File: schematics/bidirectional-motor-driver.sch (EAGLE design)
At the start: 14 parts, among them IC1 4011D

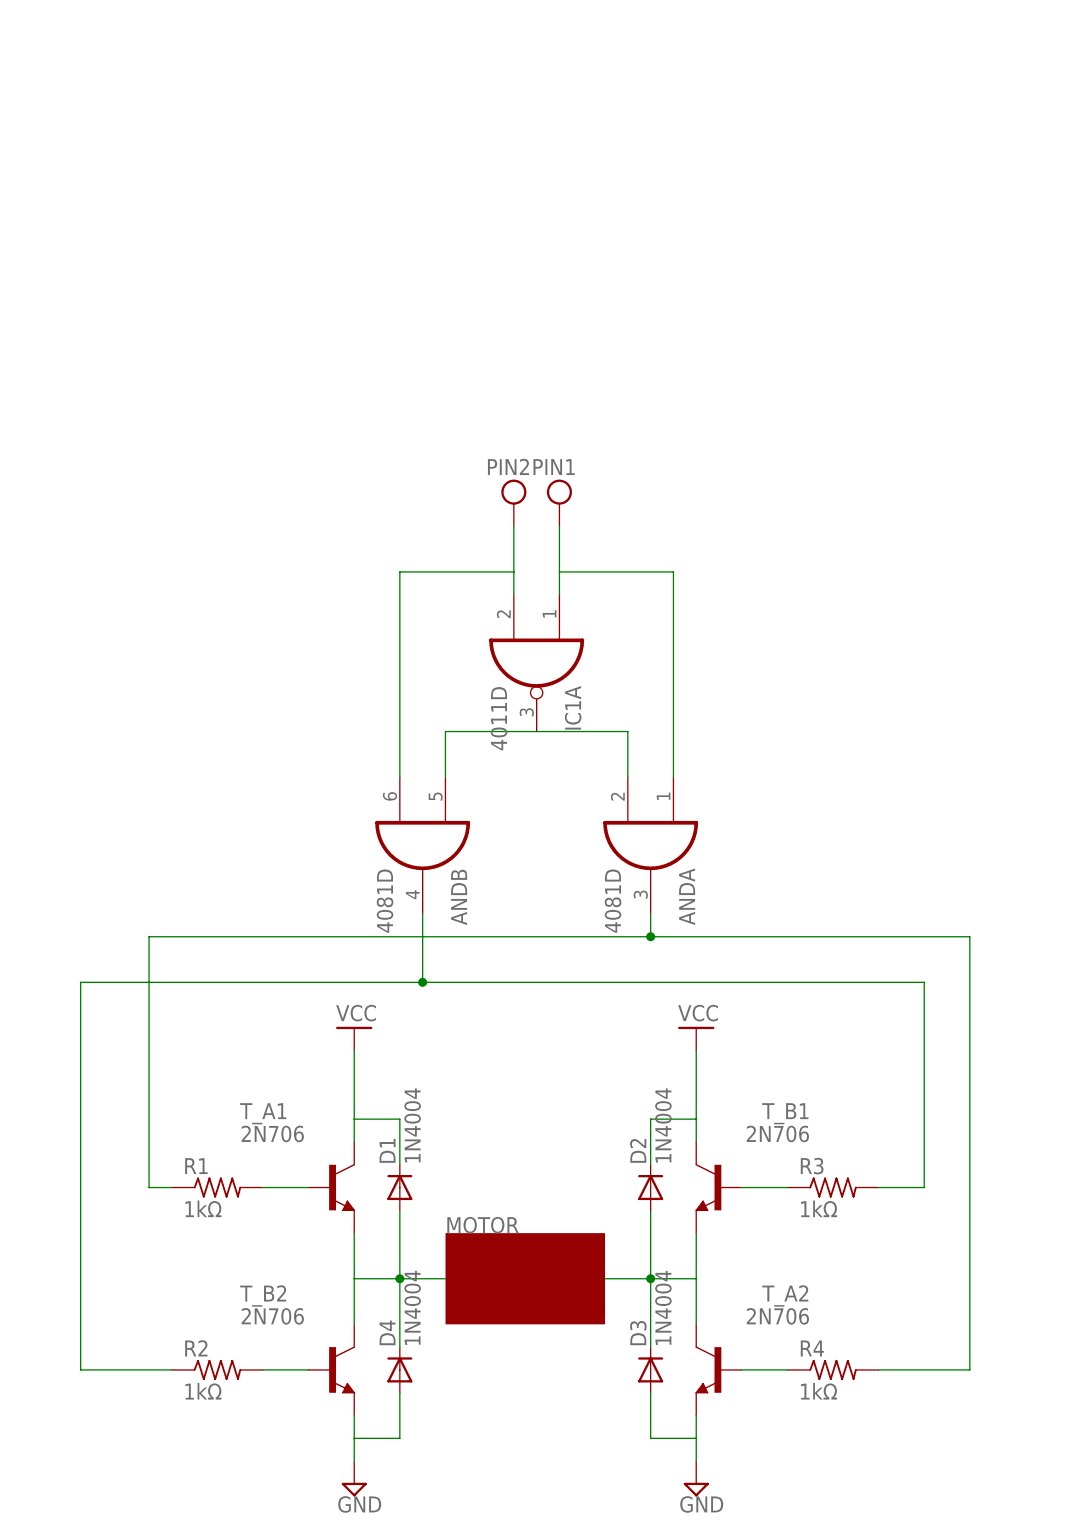
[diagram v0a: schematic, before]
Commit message: Added amplifier circuits to fix voltage for the bidirectional motor driver.
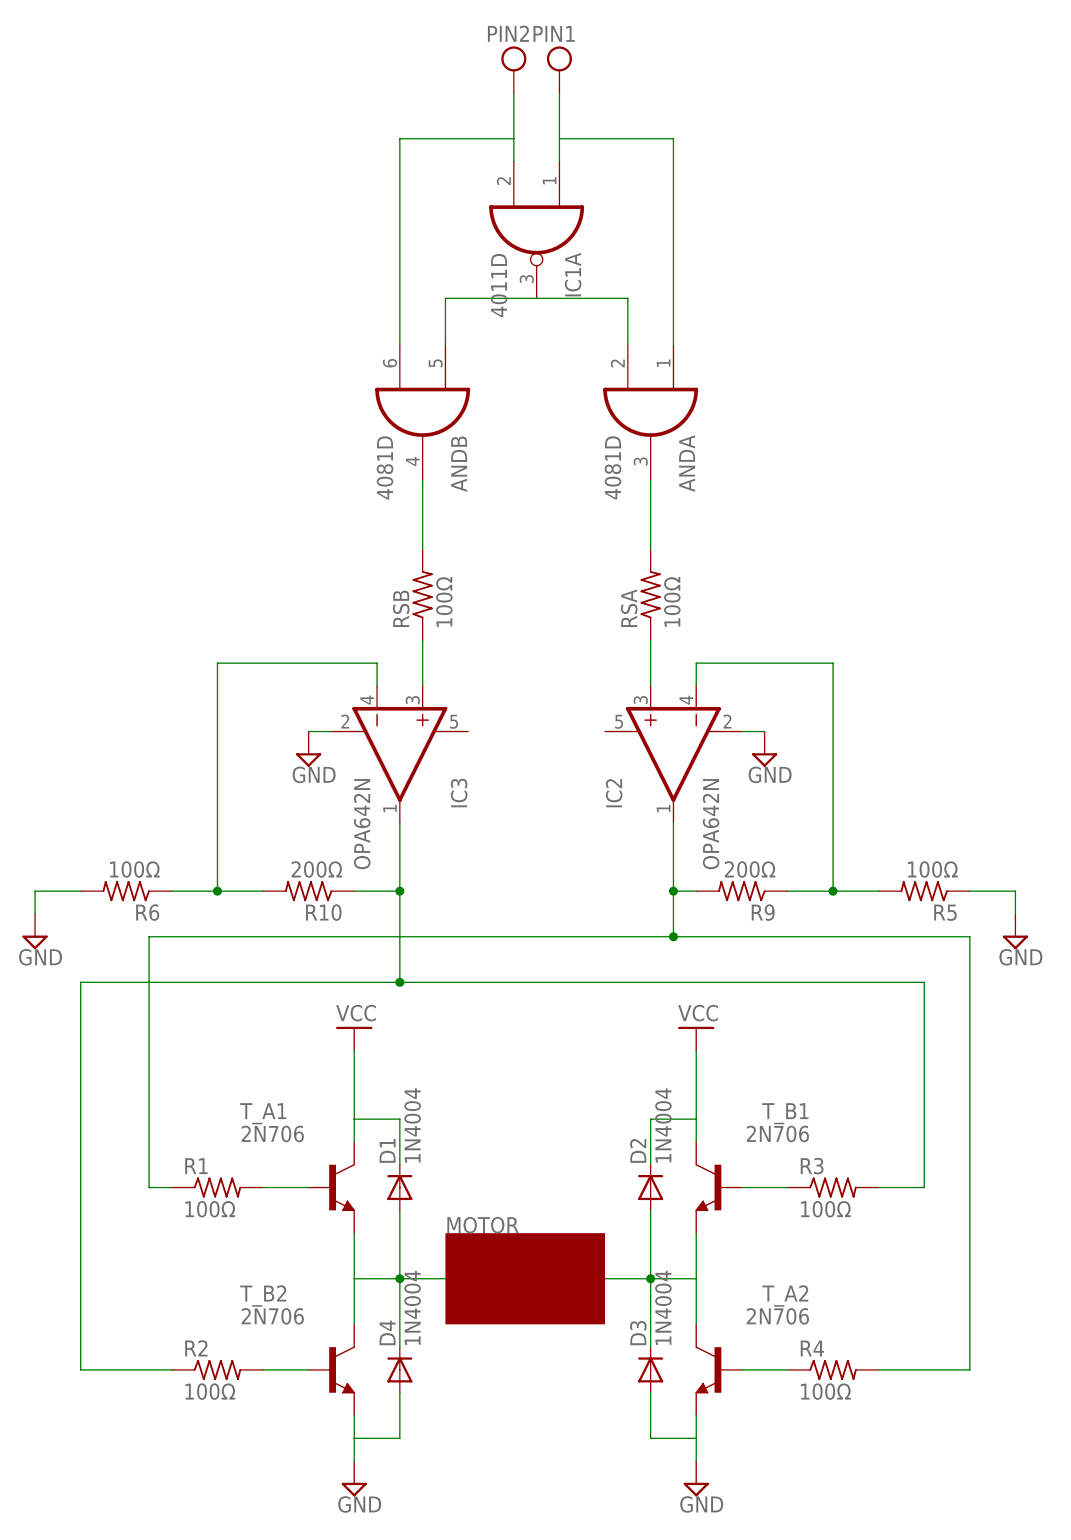
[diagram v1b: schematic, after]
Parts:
- added IC2, IC3: OPA642N, burr-brown:OPA642N
- added R10, R9: 200Ω, rcl:R-US_0204/2V
- added R5, R6, RSA, RSB: 100Ω, rcl:R-US_0204/2V
- R1, R2, R3, R4: value 1kΩ -> 100Ω
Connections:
- new net N$10: ANDB.O, RSB.2
- new net N$11: ANDA.O, RSA.2
- new net N$12: IC2.+IN, RSA.1
- new net N$13: IC3.+IN, RSB.1
- new net N$14: IC3.-IN, R10.2, R6.1
- new net N$15: IC2.-IN, R5.2, R9.1
- net GND: now also IC2.V-, IC3.V-, R5.1, R6.2
- net N$8: now also IC3.OUT, R10.1; no longer ANDB.O
- net N$9: now also IC2.OUT, R9.2; no longer ANDA.O
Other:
- moved on the sheet: ANDA, ANDB, IC1A

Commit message: Worked on final proposal, started high-level diagram of circuitry.  Need button circuitry; will finish at next meeting.
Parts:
- removed AND: 4081D, 40xx:4081D
- removed D1, D2, D3, D4: 1N4004, diode:1N4004
- removed IC1: 4011D, 40xx:4011D
- removed IC2, IC3: OPA642N, burr-brown:OPA642N
- removed R1, R2, R3, R4, R5, R6, RSA, RSB: 100Ω, rcl:R-US_0204/2V
- removed R10, R9: 200Ω, rcl:R-US_0204/2V
- removed T_A1, T_A2, T_B1, T_B2: 2N706, transistor:2N706
- added AND1: 4081D, 40xx:4081D
- added D5, D6, D7, D8: 1N4004, diode:1N4004
- added IC4: NAND, 40xx:4011D
- added IC5, IC6: OPA642N, burr-brown:OPA642N
- added R11, R12, R13, R14, R7, R8, RSA1, RSB1: 100Ω, rcl:R-US_0204/2V
- added R15, R16: 200Ω, rcl:R-US_0204/2V
- added T_A3, T_A4, T_B3, T_B4: 2N706, transistor:2N706
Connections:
- removed net N$1: D2.A, D3.C, T_A2.C, T_B1.E
- removed net N$10: ANDB.O, RSB.2
- removed net N$11: ANDA.O, RSA.2
- removed net N$12: IC2.+IN, RSA.1
- removed net N$13: IC3.+IN, RSB.1
- removed net N$14: IC3.-IN, R10.2, R6.1
- removed net N$15: IC2.-IN, R5.2, R9.1
- removed net N$2: D1.A, D4.C, T_A1.E, T_B2.C
- removed net N$3: R4.1, T_A2.B
- removed net N$4: R3.1, T_B1.B
- removed net N$5: R1.2, T_A1.B
- removed net N$6: R2.2, T_B2.B
- removed net N$7: ANDA.I1, ANDB.I0, IC1A.O
- removed net N$8: IC3.OUT, R10.1, R2.1, R3.2
- removed net N$9: IC2.OUT, R1.1, R4.2, R9.2
- new net N$20: D6.A, D7.C, T_A4.C, T_B4.E
- new net N$21: D5.A, D8.C, T_A3.E, T_B3.C
- new net N$22: R12.1, T_A4.B
- new net N$23: R11.1, T_B4.B
- new net N$24: R8.2, T_A3.B
- new net N$25: R7.2, T_B3.B
- new net N$26: AND1A.I1, AND1B.I0, IC4A.O
- new net N$27: IC6.OUT, R11.2, R7.1
- new net N$28: IC5.OUT, R12.2, R8.1
- new net N$29: AND1B.O, RSB1.2
- new net N$30: AND1A.O, RSA1.2
- new net N$31: IC5.+IN, RSA1.1
- new net N$32: IC6.+IN, RSB1.1
- new net N$33: IC6.-IN
- new net N$34: IC5.-IN
- new net N$35: IC5.V+, IC6.V+
- new net N$36: R14.1, R16.2
- new net N$37: R13.2, R15.1
- new net N$38: R15.2
- new net N$39: R16.1
- net GND: now also D7.A, D8.A, IC5.V-, IC6.V-, R13.1, R14.2, T_A4.E, T_B3.E; no longer D3.A, D4.A, IC2.V-, IC3.V-, R5.1, R6.2, T_A2.E, T_B2.E
- net VCC: now also D5.C, D6.C, T_A3.C, T_B4.C; no longer D1.C, D2.C, T_A1.C, T_B1.C
- net VDD: now also AND1A.I0, AND1B.I1, IC4A.I0, IC4A.I1; no longer ANDA.I0, ANDB.I1, IC1A.I0, IC1A.I1

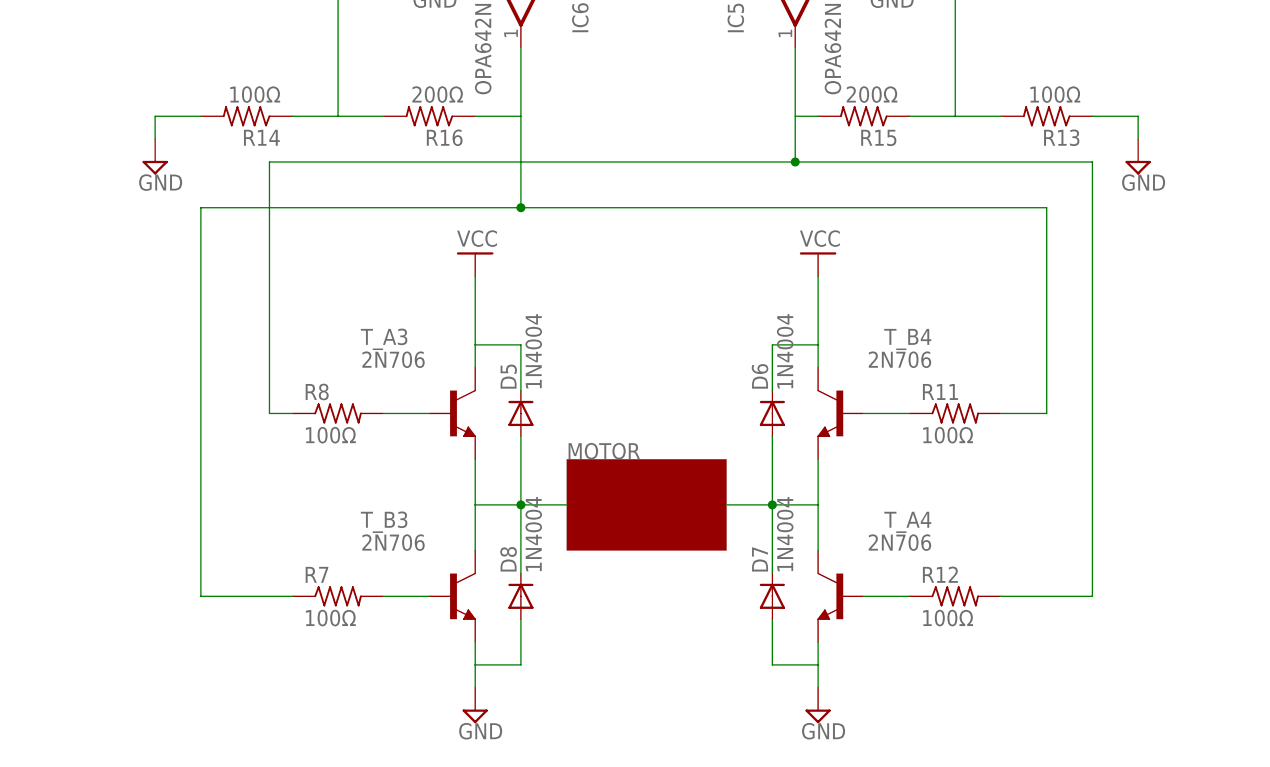
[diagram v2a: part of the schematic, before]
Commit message: Finalized the H-bridge schematic, need to convert pdfs to images and add them to the final report.
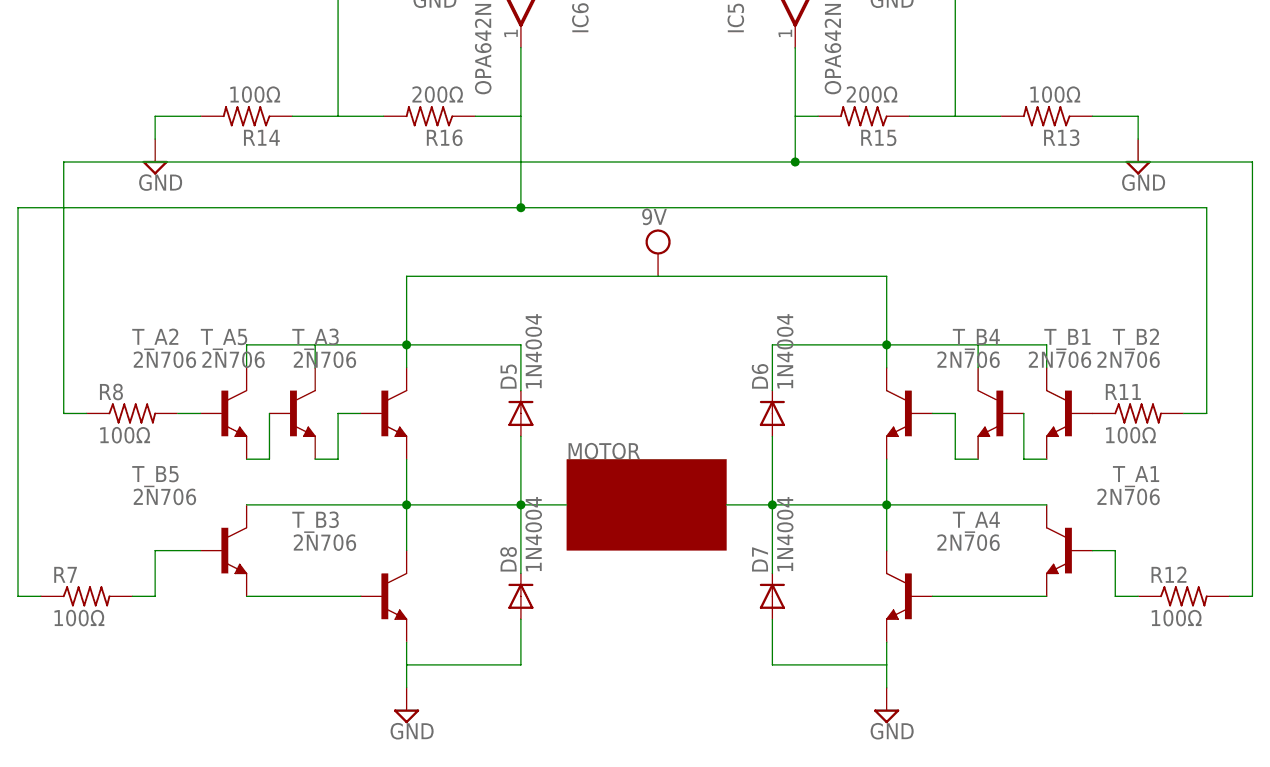
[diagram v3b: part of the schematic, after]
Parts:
- added T_A1, T_A2, T_A5, T_B1, T_B2, T_B5: 2N706, transistor:2N706
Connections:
- removed net N$22: R12.1, T_A4.B
- removed net N$23: R11.1, T_B4.B
- removed net N$24: R8.2, T_A3.B
- removed net N$25: R7.2, T_B3.B
- new net N$1: R7.2, T_B5.B
- new net N$10: T_A3.B, T_A5.E
- new net N$2: T_B3.B, T_B5.E
- new net N$3: T_A1.E, T_A4.B
- new net N$4: R12.1, T_A1.B
- new net N$5: R8.2, T_A2.B
- new net N$6: R11.1, T_B2.B
- new net N$7: T_B1.B, T_B2.E
- new net N$8: T_B1.E, T_B4.B
- new net N$9: T_A2.E, T_A5.B
- net N$20: now also T_A1.C
- net N$21: now also T_B5.C
- net VCC: now also T_A2.C, T_A5.C, T_B1.C, T_B2.C
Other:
- moved on the sheet: R11, R12, R7, R8, T_A3, T_A4, T_B3, T_B4
